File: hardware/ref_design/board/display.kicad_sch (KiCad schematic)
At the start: 29 parts, among them J3 FH12-50S-0.5SH(55), Q5 AO3400A, Q6 AO3400A, U6 MCP6002

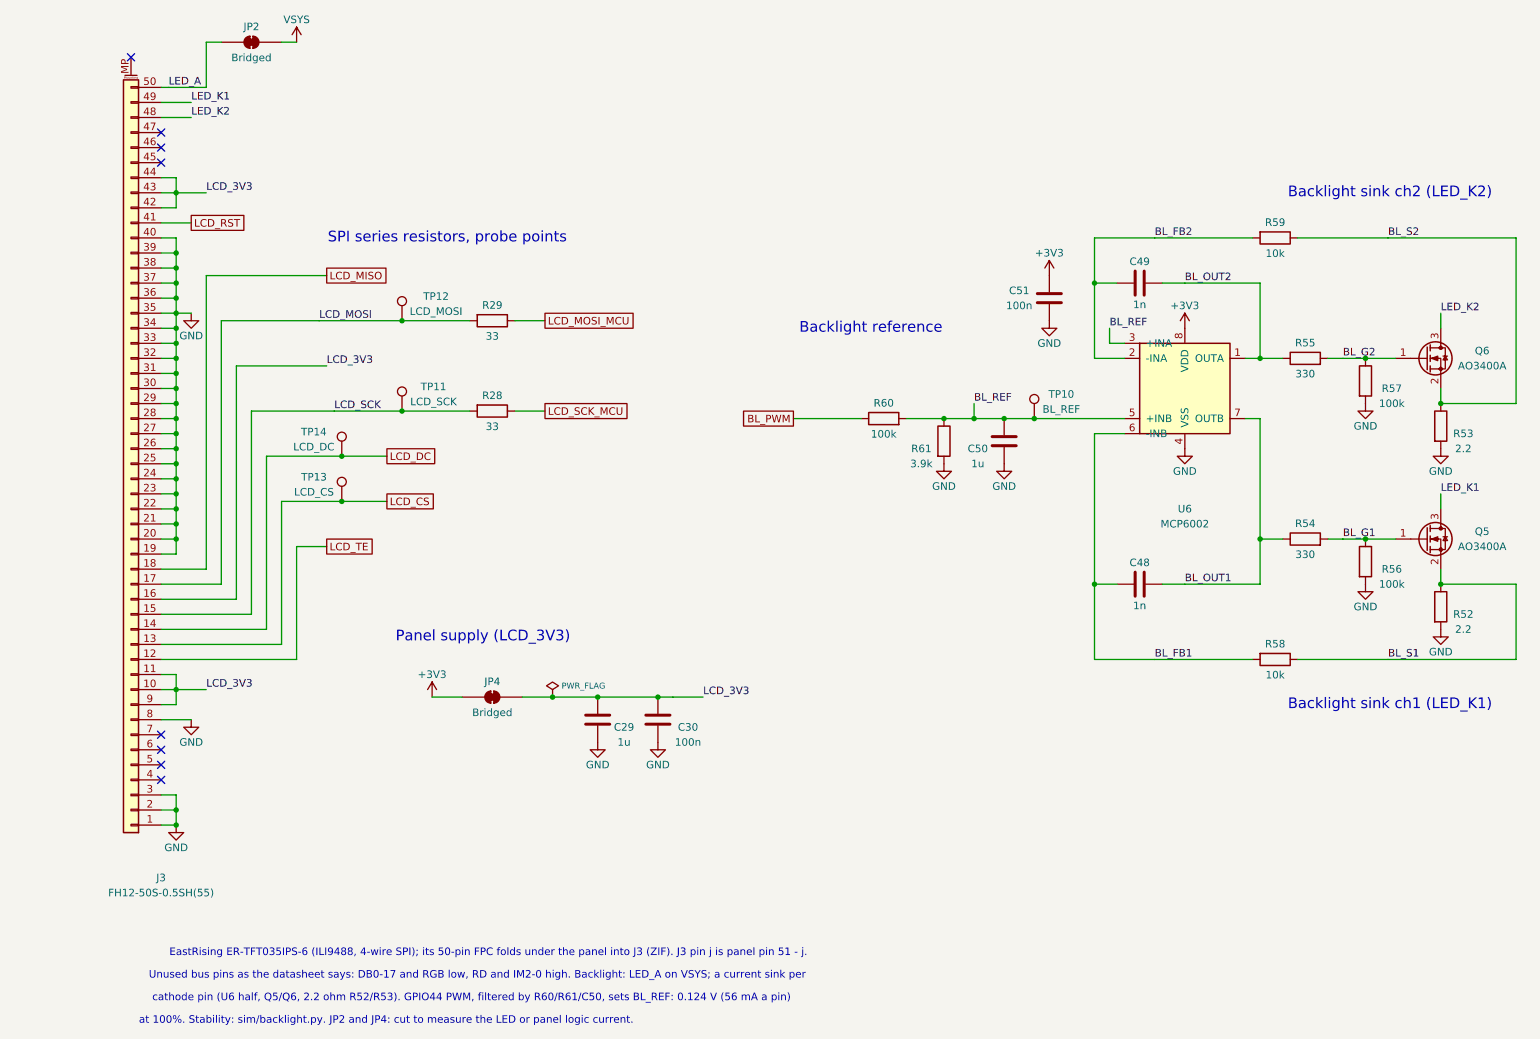
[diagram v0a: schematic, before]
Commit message: ref_design: ER-TFT024IPS-3 panel pin map, R61 2.4k
The 2.4in ST7789V panel on the same 50-pin FPC: K3/K4 on pins 4-5 join
K1/K2's sinks (two LEDs a sink), IM3-0 on pins 6-9 strapped 1110 (4-line
serial II, SDI in and SDO out, as before), D/CX on 36 and SCL on 37.
R61 3.9k -> 2.4k: 0.077 V on 2.2 ohm, 35 mA a sink, 70 mA in all (the
panel's typical, 80 max). Pin review, schematic notes and docs follow.

Co-Authored-By: Claude Opus 5.5 <noreply@anthropic.com>
Claude-Session: https://claude.ai/code/session_01Y3mFMxLYqNeyyedvbYuRwX
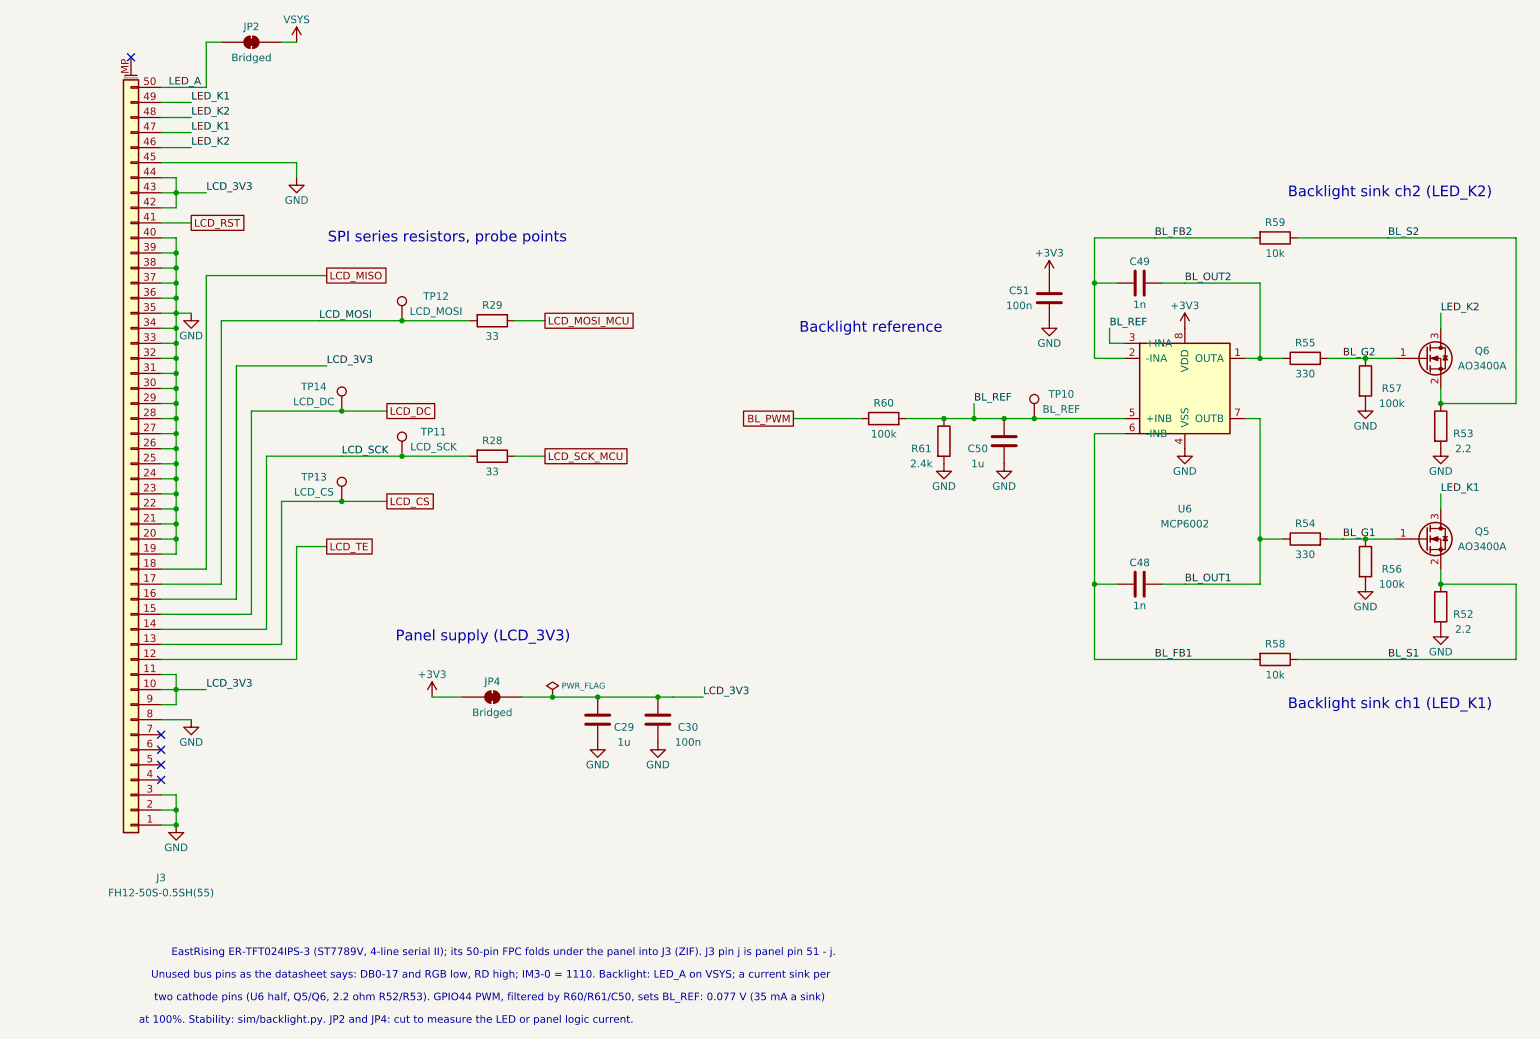
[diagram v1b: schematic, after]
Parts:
- R61: value 3.9k -> 2.4k; LCSC C51721 -> C25882; MPN 0402WGF3901TCE -> 0402WGF2401TCE
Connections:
- net GND: now also J3.45 (Pin_45)
- net LCD_DC: now also J3.15 (Pin_15); no longer J3.14 (Pin_14)
- net LCD_SCK: now also J3.14 (Pin_14); no longer J3.15 (Pin_15)
- net LED_K1: now also J3.47 (Pin_47)
- net LED_K2: now also J3.46 (Pin_46)
- no-connect marks 8 -> 5
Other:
- note added: "EastRising ER-TFT024IPS-3 (ST7789V, 4-line serial II); its 50-pin FPC folds under the panel into J3 (ZIF). J3 pin j is panel pin 51 - j."
- note added: "Unused bus pins as the datasheet says: DB0-17 and RGB low, RD high; IM3-0 = 1110. Backlight: LED_A on VSYS; a current sink per"
- note added: "two cathode pins (U6 half, Q5/Q6, 2.2 ohm R52/R53). GPIO44 PWM, filtered by R60/R61/C50, sets BL_REF: 0.077 V (35 mA a sink)"
- note removed: "EastRising ER-TFT035IPS-6 (ILI9488, 4-wire SPI); its 50-pin FPC folds under the panel into J3 (ZIF). J3 pin j is panel pin 51 - j."
- note removed: "Unused bus pins as the datasheet says: DB0-17 and RGB low, RD and IM2-0 high. Backlight: LED_A on VSYS; a current sink per"
- note removed: "cathode pin (U6 half, Q5/Q6, 2.2 ohm R52/R53). GPIO44 PWM, filtered by R60/R61/C50, sets BL_REF: 0.124 V (56 mA a pin)"
- moved on the sheet: R28, TP11, TP14

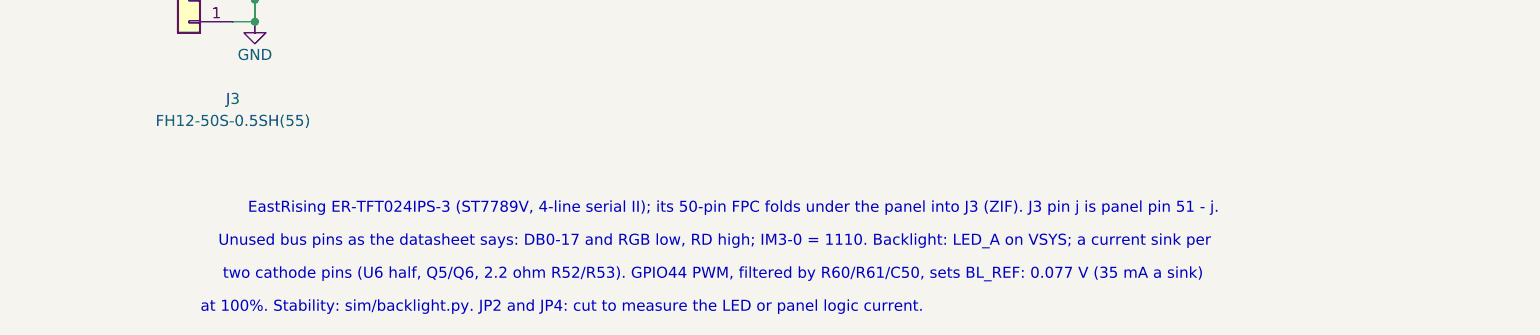
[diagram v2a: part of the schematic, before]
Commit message: ref_design levers: pins facing their nets, no REV straps, no UART, debug buttons and latch parts out of the strips
An experiment for Alex (not on ref-design-cellcut): make the board easier to route without
changing its size.
1. GPIOs: AUDIO_PWM 8 -> 31 (PWM7 B), AMP_EN 11 -> 34, BL_PWM 44 -> 28 (PWM6 A), PWR_HOLD
   2 -> 44, P2_START 34 -> 2, P2_SELECT 9 -> 4, SR_PL 28 -> 19 (datasheet Table 3 checked;
   U4's pin review updated)
2. REV0-REV3 and R48-R51 removed (the revision stays on the silkscreen)
3. J6 (UART) and C41 removed; SW18/SW19 out of the left strip into the left bezel below H4
   (U3 and its caps 2 mm down, JP1 below the core)
4. The latch's strip parts (Q1, R16, R15, C47, TP6, D8, Q7, R62, R63) up past the hole's
   top edge under seat 2's deck; C42 to the right bezel
tools/strip_load.py counts nets through each strip: 11/15 -> 8/11, parts 8/16 -> 3/5.
Routed clean on the first finished attempt (seed 3, 4.2 min); check_pcb and check_fit pass.

Co-Authored-By: Claude Opus 5.5 <noreply@anthropic.com>
Claude-Session: https://claude.ai/code/session_01Y3mFMxLYqNeyyedvbYuRwX
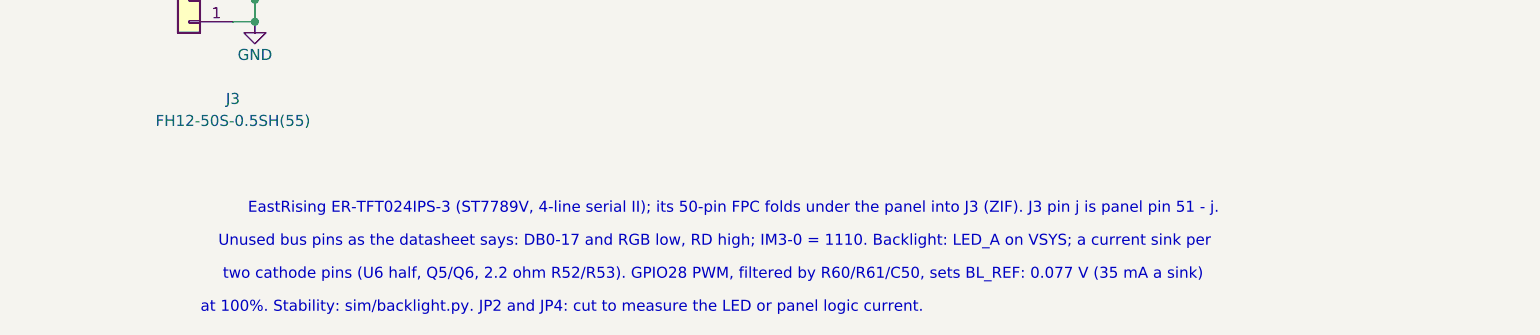
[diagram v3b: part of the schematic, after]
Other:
- note added: "two cathode pins (U6 half, Q5/Q6, 2.2 ohm R52/R53). GPIO28 PWM, filtered by R60/R61/C50, sets BL_REF: 0.077 V (35 mA a sink)"
- note removed: "two cathode pins (U6 half, Q5/Q6, 2.2 ohm R52/R53). GPIO44 PWM, filtered by R60/R61/C50, sets BL_REF: 0.077 V (35 mA a sink)"
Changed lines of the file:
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@@
 		)
 	)
-	(text "two cathode pins (U6 half, Q5/Q6, 2.2 ohm R52/R53). GPIO44 PWM, filtered by R60/R61/C50, sets BL_REF: 0.077 V (35 mA a sink)"
+	(text "two cathode pins (U6 half, Q5/Q6, 2.2 ohm R52/R53). GPIO28 PWM, filtered by R60/R61/C50, sets BL_REF: 0.077 V (35 mA a sink)"
 		(exclude_from_sim no)
 		(at 83.366 182.88 0)
@@
 		(in_pos_files yes)
 		(dnp no)
-		(property "Reference" "#PWR082"
+		(property "Reference" "#PWR076"
 			(at 50.8 21.59 0)
 			(hide yes)
@@
 			(project "battler"
 				(path "/8922e0a8-6f76-52f6-b0ec-4de6a784796f/99b2b9c1-5178-5fd9-a3fe-39987bd8b040"
-					(reference "#PWR082")
+					(reference "#PWR076")
 					(unit 1)
 				)
@@
 		(in_pos_files yes)
 		(dnp no)
-		(property "Reference" "#PWR083"
+		(property "Reference" "#PWR077"
 			(at 50.8 44.45 0)
 			(hide yes)
@@
 			(project "battler"
 				(path "/8922e0a8-6f76-52f6-b0ec-4de6a784796f/99b2b9c1-5178-5fd9-a3fe-39987bd8b040"
-					(reference "#PWR083")
+					(reference "#PWR077")
 					(unit 1)
 				)
@@
 		(in_pos_files yes)
 		(dnp no)
-		(property "Reference" "#PWR084"
+		(property "Reference" "#PWR078"
 			(at 33.02 67.31 0)
 			(hide yes)
@@
 			(project "battler"
 				(path "/8922e0a8-6f76-52f6-b0ec-4de6a784796f/99b2b9c1-5178-5fd9-a3fe-39987bd8b040"
-					(reference "#PWR084")
+					(reference "#PWR078")
 					(unit 1)
 				)
@@
 		(in_pos_files yes)
 		(dnp no)
-		(property "Reference" "#PWR085"
+		(property "Reference" "#PWR079"
 			(at 33.02 135.89 0)
 			(hide yes)
@@
 			(project "battler"
 				(path "/8922e0a8-6f76-52f6-b0ec-4de6a784796f/99b2b9c1-5178-5fd9-a3fe-39987bd8b040"
-					(reference "#PWR085")
+					(reference "#PWR079")
 					(unit 1)
 				)
@@
 		(in_pos_files yes)
 		(dnp no)
-		(property "Reference" "#PWR086"
+		(property "Reference" "#PWR080"
 			(at 30.48 153.67 0)
 			(hide yes)
@@
 			(project "battler"
 				(path "/8922e0a8-6f76-52f6-b0ec-4de6a784796f/99b2b9c1-5178-5fd9-a3fe-39987bd8b040"
-					(reference "#PWR086")
+					(reference "#PWR080")
 					(unit 1)
 				)
@@
 		(in_pos_files yes)
 		(dnp no)
-		(property "Reference" "#PWR087"
+		(property "Reference" "#PWR081"
 			(at 73.66 132.08 0)
 			(hide yes)
@@
 			(project "battler"
 				(path "/8922e0a8-6f76-52f6-b0ec-4de6a784796f/99b2b9c1-5178-5fd9-a3fe-39987bd8b040"
-					(reference "#PWR087")
+					(reference "#PWR081")
 					(unit 1)
 				)
@@
 		(in_pos_files yes)
 		(dnp no)
-		(property "Reference" "#PWR088"
+		(property "Reference" "#PWR082"
 			(at 101.6 139.7 0)
 			(hide yes)
@@
 			(project "battler"
 				(path "/8922e0a8-6f76-52f6-b0ec-4de6a784796f/99b2b9c1-5178-5fd9-a3fe-39987bd8b040"
-					(reference "#PWR088")
+					(reference "#PWR082")
 					(unit 1)
 				)
@@
 		(in_pos_files yes)
 		(dnp no)
-		(property "Reference" "#PWR089"
+		(property "Reference" "#PWR083"
 			(at 111.76 139.7 0)
 			(hide yes)
@@
 			(project "battler"
 				(path "/8922e0a8-6f76-52f6-b0ec-4de6a784796f/99b2b9c1-5178-5fd9-a3fe-39987bd8b040"
-					(reference "#PWR089")
+					(reference "#PWR083")
 					(unit 1)
 				)
@@
 		(in_pos_files yes)
 		(dnp no)
-		(property "Reference" "#PWR090"
+		(property "Reference" "#PWR084"
 			(at 160.02 92.71 0)
 			(hide yes)
@@
 			(project "battler"
 				(path "/8922e0a8-6f76-52f6-b0ec-4de6a784796f/99b2b9c1-5178-5fd9-a3fe-39987bd8b040"
-					(reference "#PWR090")
+					(reference "#PWR084")
 					(unit 1)
 				)
@@
 		(in_pos_files yes)
 		(dnp no)
-		(property "Reference" "#PWR091"
+		(property "Reference" "#PWR085"
 			(at 170.18 92.71 0)
 			(hide yes)
@@
 			(project "battler"
 				(path "/8922e0a8-6f76-52f6-b0ec-4de6a784796f/99b2b9c1-5178-5fd9-a3fe-39987bd8b040"
-					(reference "#PWR091")
+					(reference "#PWR085")
 					(unit 1)
 				)
@@
 		(in_pos_files yes)
 		(dnp no)
-		(property "Reference" "#PWR092"
+		(property "Reference" "#PWR086"
 			(at 177.8 60.96 0)
 			(hide yes)
@@
 			(project "battler"
 				(path "/8922e0a8-6f76-52f6-b0ec-4de6a784796f/99b2b9c1-5178-5fd9-a3fe-39987bd8b040"
-					(reference "#PWR092")
+					(reference "#PWR086")
 					(unit 1)
 				)
@@
 		(in_pos_files yes)
 		(dnp no)
-		(property "Reference" "#PWR093"
+		(property "Reference" "#PWR087"
 			(at 177.8 68.58 0)
 			(hide yes)
@@
 			(project "battler"
 				(path "/8922e0a8-6f76-52f6-b0ec-4de6a784796f/99b2b9c1-5178-5fd9-a3fe-39987bd8b040"
-					(reference "#PWR093")
+					(reference "#PWR087")
 					(unit 1)
 				)
@@
 		(in_pos_files yes)
 		(dnp no)
-		(property "Reference" "#PWR094"
+		(property "Reference" "#PWR088"
 			(at 200.66 69.85 0)
 			(hide yes)
@@
 			(project "battler"
 				(path "/8922e0a8-6f76-52f6-b0ec-4de6a784796f/99b2b9c1-5178-5fd9-a3fe-39987bd8b040"
-					(reference "#PWR094")
+					(reference "#PWR088")
 					(unit 1)
 				)
@@
 		(in_pos_files yes)
 		(dnp no)
-		(property "Reference" "#PWR095"
+		(property "Reference" "#PWR089"
 			(at 200.66 90.17 0)
 			(hide yes)
@@
 			(project "battler"
 				(path "/8922e0a8-6f76-52f6-b0ec-4de6a784796f/99b2b9c1-5178-5fd9-a3fe-39987bd8b040"
-					(reference "#PWR095")
+					(reference "#PWR089")
 					(unit 1)
 				)
@@
 		(in_pos_files yes)
 		(dnp no)
-		(property "Reference" "#PWR096"
+		(property "Reference" "#PWR090"
 			(at 231.14 82.55 0)
 			(hide yes)
@@
 			(project "battler"
 				(path "/8922e0a8-6f76-52f6-b0ec-4de6a784796f/99b2b9c1-5178-5fd9-a3fe-39987bd8b040"
-					(reference "#PWR096")
+					(reference "#PWR090")
 					(unit 1)
 				)
@@
 		(in_pos_files yes)
 		(dnp no)
-		(property "Reference" "#PWR097"
+		(property "Reference" "#PWR091"
 			(at 243.84 90.17 0)
 			(hide yes)
@@
 			(project "battler"
 				(path "/8922e0a8-6f76-52f6-b0ec-4de6a784796f/99b2b9c1-5178-5fd9-a3fe-39987bd8b040"
-					(reference "#PWR097")
+					(reference "#PWR091")
 					(unit 1)
 				)
@@
 		(in_pos_files yes)
 		(dnp no)
-		(property "Reference" "#PWR098"
+		(property "Reference" "#PWR092"
 			(at 231.14 113.03 0)
 			(hide yes)
@@
 			(project "battler"
 				(path "/8922e0a8-6f76-52f6-b0ec-4de6a784796f/99b2b9c1-5178-5fd9-a3fe-39987bd8b040"
-					(reference "#PWR098")
+					(reference "#PWR092")
 					(unit 1)
 				)
@@
 		(in_pos_files yes)
 		(dnp no)
-		(property "Reference" "#PWR099"
+		(property "Reference" "#PWR093"
 			(at 243.84 120.65 0)
 			(hide yes)
@@
 			(project "battler"
 				(path "/8922e0a8-6f76-52f6-b0ec-4de6a784796f/99b2b9c1-5178-5fd9-a3fe-39987bd8b040"
-					(reference "#PWR099")
+					(reference "#PWR093")
 					(unit 1)
 				)
